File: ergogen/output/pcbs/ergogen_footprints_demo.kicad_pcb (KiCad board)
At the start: 2 copper layers, 99.5 x 99.5 mm, 30 parts

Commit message: Refresh output
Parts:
- added DISP1, DISP2: , ceoloide:nice_view, F.Cu at (75.0, 75.0)
- added DISP3, DISP4, DISP5: , ceoloide:display_ssd1306_nice_view, F.Cu at (75.0, 75.0)
- added JST1: , ceoloide/battery_connector_jst_ph_2, F.Cu at (75.0, 75.0)
- added LED1: , ceoloide:led_SK6812mini-e (per-keysingle-side), B.Cu at (55.0, 50.3)
- added LED2: , ceoloide:led_SK6812mini-e (per-key, reversible), B.Cu at (55.0, 70.3)
- added LED3: , ceoloide:led_SK6812mini-e (underglow, reversible), B.Cu at (35.0, 70.3)
- added LED4: , ceoloide:led_SK6812mini-e (underglowsingle-side), B.Cu at (35.0, 30.3)
- added MCU1, MCU2: , ceoloide:nice_nano, F.Cu at (75.0, 75.0)
- added MH1, MH2: , ceoloide:mounting_hole_npth, F.Cu at (75.0, 75.0)
- added PWR1, PWR2: reset_button, ceoloide:power_switch_smd_side, F.Cu at (75.0, 75.0)
- added RST1, RST2: reset_button_smd_side, ceoloide:reset_button_smd_side, F.Cu at (75.0, 75.0)
- added RST3: reset_switch_tht_top, ceoloide:reset_switch_tht_top, F.Cu at (75.0, 75.0)
- added TRRS1: TRRS-PJ-320A-dual, ceoloide:trrs_pj320a (reversible), F.Cu at (75.0, 75.0)
- added TRRS2: TRRS-PJ-320A-dual, ceoloide:trrs_pj320a (reversible, symmetric), F.Cu at (75.0, 75.0)
- added TRRS3: TRRS-PJ-320A-dual, ceoloide:trrs_pj320a, F.Cu at (75.0, 75.0)
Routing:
- net LED_U_1: track 0.00 -> 209.9 mm, vias 0 -> 1
- net c1_r2: track 0.00 -> 202.8 mm
- net LED_U_2: track 0.00 -> 108.5 mm, vias 0 -> 1
- net LED_U_3: track 0.00 -> 101.8 mm
- net JST1_1: track 0.00 -> 34.3 mm
- net c1_r1: track 0.00 -> 30.7 mm
- net GND: track 0.00 -> 17.3 mm, vias 0 -> 2
- net SDA: track 0.00 -> 9.80 mm
- net SCL: track 0.00 -> 9.80 mm
- net CS: track 0.00 -> 9.80 mm
- net VCC: track 0.00 -> 7.51 mm, vias 0 -> 2
- net LED_1: track 0.00 -> 6.76 mm, vias 0 -> 1
- net LED: track 0.00 -> 6.76 mm, vias 0 -> 1
- net JST1_2: track 0.00 -> 3.60 mm
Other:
- board text added: "JLCJLCJLCJLC"

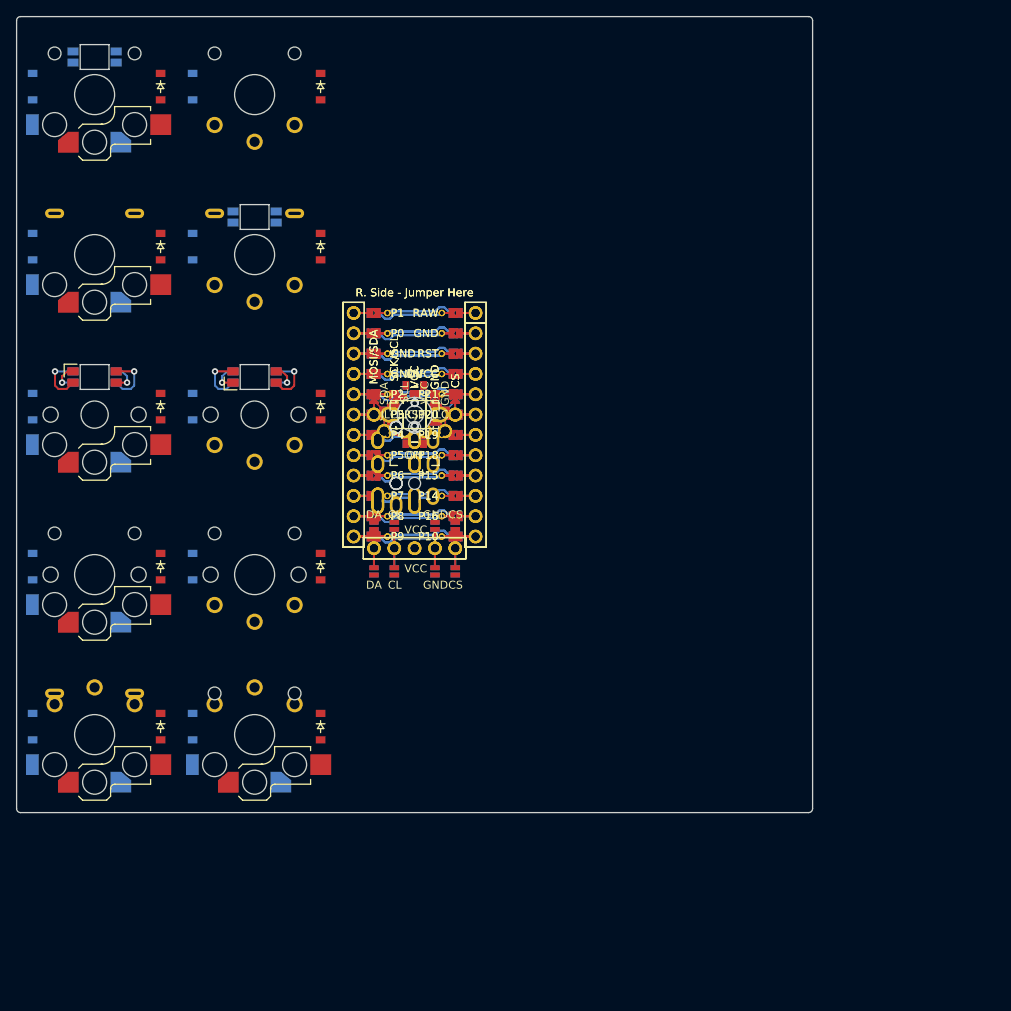
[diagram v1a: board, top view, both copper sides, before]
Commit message: Add some rotation and shift to test footprints
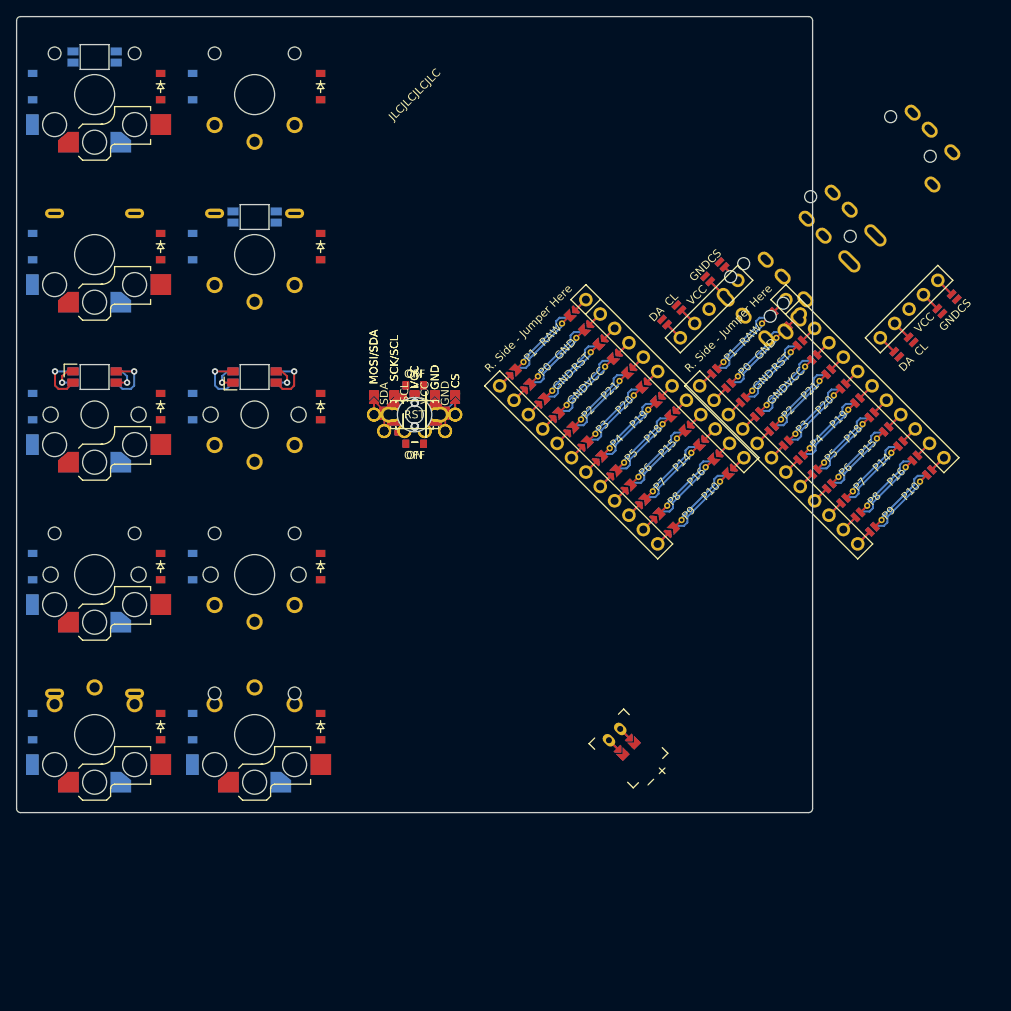
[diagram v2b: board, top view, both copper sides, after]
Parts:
- moved TRRS3 72.1 mm to (135.0, 35.0), turned to 45 degrees
- moved TRRS2 58.3 mm to (125.0, 45.0), turned to 45 degrees
- moved DISP2 55.9 mm to (125.0, 50.0), turned to 45 degrees
- moved MCU2 50.0 mm to (125.0, 75.0), turned to 45 degrees
- moved JST1 47.2 mm to (100.0, 115.0), turned to 45 degrees
- moved TRRS1 44.7 mm to (115.0, 55.0), turned to 45 degrees
- moved DISP1 35.4 mm to (100.0, 50.0), turned to 45 degrees
- moved MCU1 25.0 mm to (100.0, 75.0), turned to 45 degrees

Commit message: Adjust the position of a few components
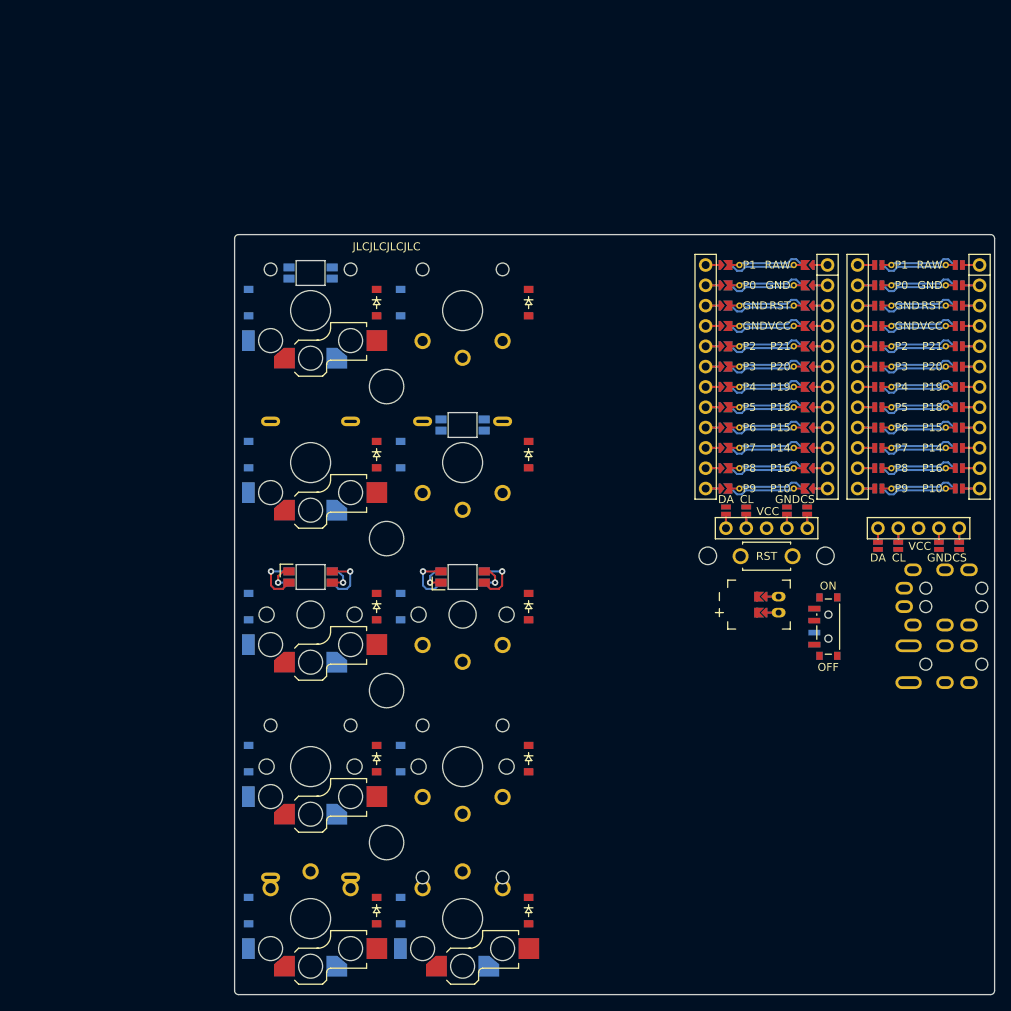
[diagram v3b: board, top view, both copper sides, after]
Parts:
- removed DISP3, DISP4, DISP5: , ceoloide:display_ssd1306_nice_view
- removed PWR2: reset_button, ceoloide:power_switch_smd_side
- removed the RST1 at (75.0, 75.0)
- removed RST2: reset_button_smd_side, ceoloide:reset_button_smd_side
- removed TRRS3: TRRS-PJ-320A-dual, ceoloide:trrs_pj320a
- added MH3: , ceoloide:mounting_hole_npth, F.Cu at (71.5, 90.5)
- added MH4: , ceoloide:mounting_hole_npth, F.Cu at (71.5, 71.5)
- added MH5: , ceoloide:mounting_hole_npth, F.Cu at (111.7, 92.7)
- added MH6: , ceoloide:mounting_hole_npth, F.Cu at (126.3, 92.7)
- moved TRRS2 67.4 mm to (147.5, 108.5), turned to -90 degrees
- moved PWR1 58.1 mm to (126.7, 101.5)
- moved TRRS1 54.7 mm to (147.5, 99.0), turned to -90 degrees
- moved MH1 53.6 mm to (71.5, 128.5)
- moved RST1 47.4 mm to (119.0, 92.7)
- moved DISP1 44.2 mm to (138.0, 72.5), turned to 0 degrees
- moved MCU1 38.5 mm to (138.0, 69.0), turned to 0 degrees
- moved D15 38.2 mm to (70.2, 61.0)
- moved D5 38.2 mm to (54.2, 61.0)
- moved S1 38.2 mm to (62.0, 62.0)
- moved LED4 38.2 mm to (62.0, 57.3)
- moved D10 37.5 mm to (73.2, 61.0)
- moved D14 37.5 mm to (70.2, 80.0)
- moved D20 37.5 mm to (89.2, 61.0)
- moved D4 37.5 mm to (54.2, 80.0)
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- renumbered RST3 to RST1
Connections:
- DISP1 pad 10: DISP1_1 -> CS
- DISP1 pad 11: DISP1_2 -> GND
- DISP1 pad 12: DISP1_4 -> SCL
- DISP1 pad 13: DISP1_5 -> SDA
- DISP1 pad 14: CS -> DISP1_1
- DISP1 pad 15: GND -> DISP1_2
- DISP1 pad 16: SCL -> DISP1_4
- DISP1 pad 17: SDA -> DISP1_5
- DISP1 pad 20: DISP1_5 -> CS
- DISP1 pad 21: DISP1_4 -> GND
- DISP1 pad 22: DISP1_2 -> SCL
- DISP1 pad 23: DISP1_1 -> SDA
- DISP1 pad 24: CS -> DISP1_5
- DISP1 pad 25: GND -> DISP1_4
- DISP1 pad 26: SCL -> DISP1_2
- DISP1 pad 27: SDA -> DISP1_1
- DISP2 pad 10: CS -> DISP2_1
- DISP2 pad 11: GND -> DISP2_2
- DISP2 pad 12: SCL -> DISP2_4
- DISP2 pad 13: SDA -> DISP2_5
- DISP2 pad 14: DISP2_1 -> CS
- DISP2 pad 15: DISP2_2 -> GND
- DISP2 pad 16: DISP2_4 -> SCL
- DISP2 pad 17: DISP2_5 -> SDA
- DISP2 pad 20: CS -> DISP2_5
- DISP2 pad 21: GND -> DISP2_4
- DISP2 pad 22: SCL -> DISP2_2
- DISP2 pad 23: SDA -> DISP2_1
- DISP2 pad 24: DISP2_5 -> CS
- DISP2 pad 25: DISP2_4 -> GND
- DISP2 pad 26: DISP2_2 -> SCL
- DISP2 pad 27: DISP2_1 -> SDA
- MCU1 pad 1: MCU1_1 -> RAW
- MCU1 pad 10: MCU1_10 -> P14
- MCU1 pad 11: MCU1_11 -> P16
- MCU1 pad 12: MCU1_12 -> P10
- MCU1 pad 13: MCU1_13 -> MCU1_12
- MCU1 pad 14: MCU1_14 -> MCU1_11
- MCU1 pad 15: MCU1_15 -> MCU1_10
- MCU1 pad 16: MCU1_16 -> MCU1_9
- MCU1 pad 17: MCU1_17 -> MCU1_8
- MCU1 pad 18: MCU1_18 -> MCU1_7
- MCU1 pad 19: MCU1_19 -> MCU1_6
- MCU1 pad 2: MCU1_2 -> GND
- MCU1 pad 20: MCU1_20 -> MCU1_5
- MCU1 pad 21: MCU1_21 -> MCU1_4
- MCU1 pad 22: MCU1_22 -> MCU1_3
- MCU1 pad 23: MCU1_23 -> MCU1_2
- MCU1 pad 24: MCU1_24 -> MCU1_1
- MCU1 pad 3: MCU1_3 -> RST
- MCU1 pad 4: MCU1_4 -> VCC
- MCU1 pad 5: MCU1_5 -> P21
- MCU1 pad 6: MCU1_6 -> P20
- MCU1 pad 7: MCU1_7 -> P19
- MCU1 pad 8: MCU1_8 -> P18
- MCU1 pad 9: MCU1_9 -> P15
- MCU2 pad 1: RAW -> MCU2_1
- MCU2 pad 10: P14 -> MCU2_10
- MCU2 pad 11: P16 -> MCU2_11
- MCU2 pad 12: P10 -> MCU2_12
- MCU2 pad 13: MCU2_12 -> MCU2_13
- MCU2 pad 14: MCU2_11 -> MCU2_14
- MCU2 pad 15: MCU2_10 -> MCU2_15
- MCU2 pad 16: MCU2_9 -> MCU2_16
- MCU2 pad 17: MCU2_8 -> MCU2_17
- MCU2 pad 18: MCU2_7 -> MCU2_18
- MCU2 pad 19: MCU2_6 -> MCU2_19
- MCU2 pad 2: GND -> MCU2_2
- MCU2 pad 20: MCU2_5 -> MCU2_20
- MCU2 pad 21: MCU2_4 -> MCU2_21
- MCU2 pad 22: MCU2_3 -> MCU2_22
- MCU2 pad 23: MCU2_2 -> MCU2_23
- MCU2 pad 24: MCU2_1 -> MCU2_24
- MCU2 pad 3: RST -> MCU2_3
- MCU2 pad 4: VCC -> MCU2_4
- MCU2 pad 5: P21 -> MCU2_5
- MCU2 pad 6: P20 -> MCU2_6
- MCU2 pad 7: P19 -> MCU2_7
- MCU2 pad 8: P18 -> MCU2_8
- MCU2 pad 9: P15 -> MCU2_9
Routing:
- net P21: track 0.00 -> 203.1 mm
- net LED_U_1: track 209.9 -> 6.76 mm
- net P18: track 0.00 -> 101.8 mm
- net P15: track 0.00 -> 101.8 mm
- net LED_U_3: track 101.8 -> 0.00 mm
- net LED_U_2: track 108.5 -> 6.76 mm
- net JST1_1: track 34.3 -> 3.60 mm
- net GND: track 17.3 -> 45.2 mm
- net SCL: track 9.80 -> 7.00 mm
- net CS: track 9.80 -> 7.00 mm
- net SDA: track 9.80 -> 7.00 mm
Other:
- board size 99.5 x 99.5 mm -> 95 x 95 mm

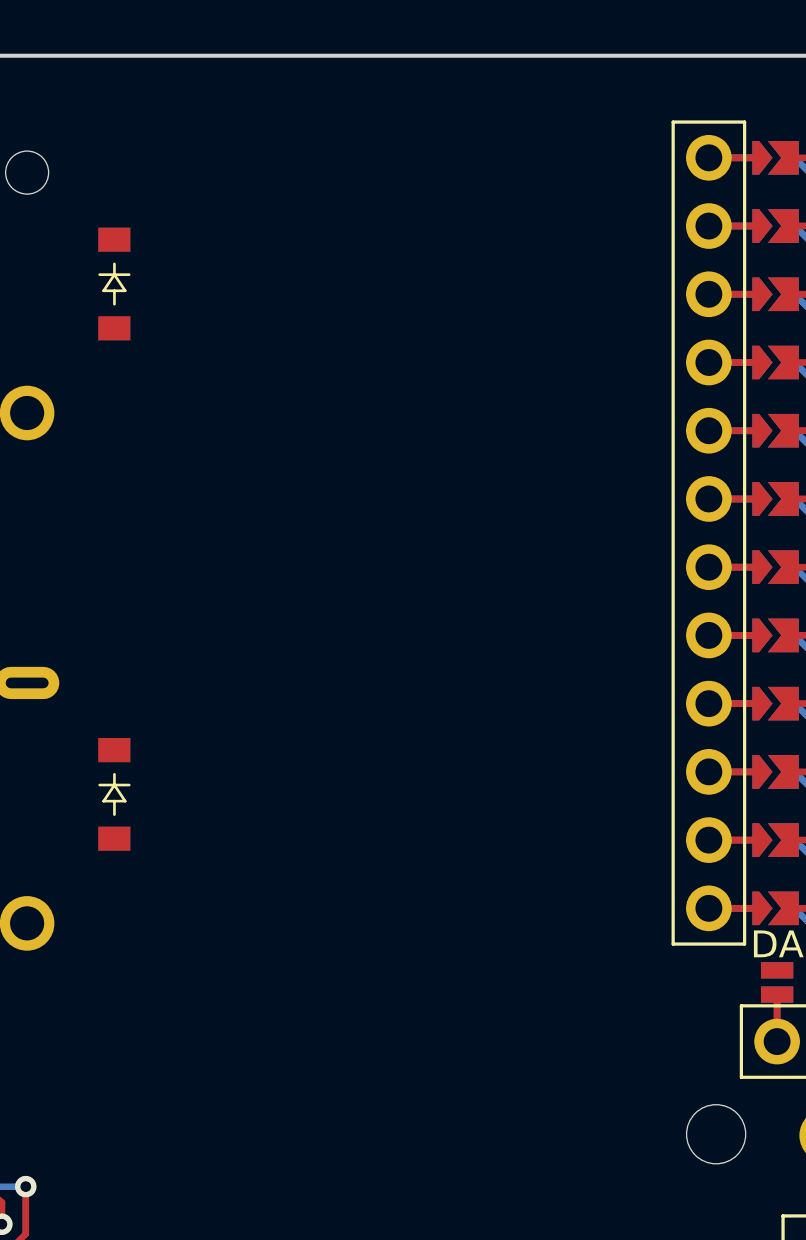
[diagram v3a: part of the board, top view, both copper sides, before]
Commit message: Add nice_nano with only required jumpers
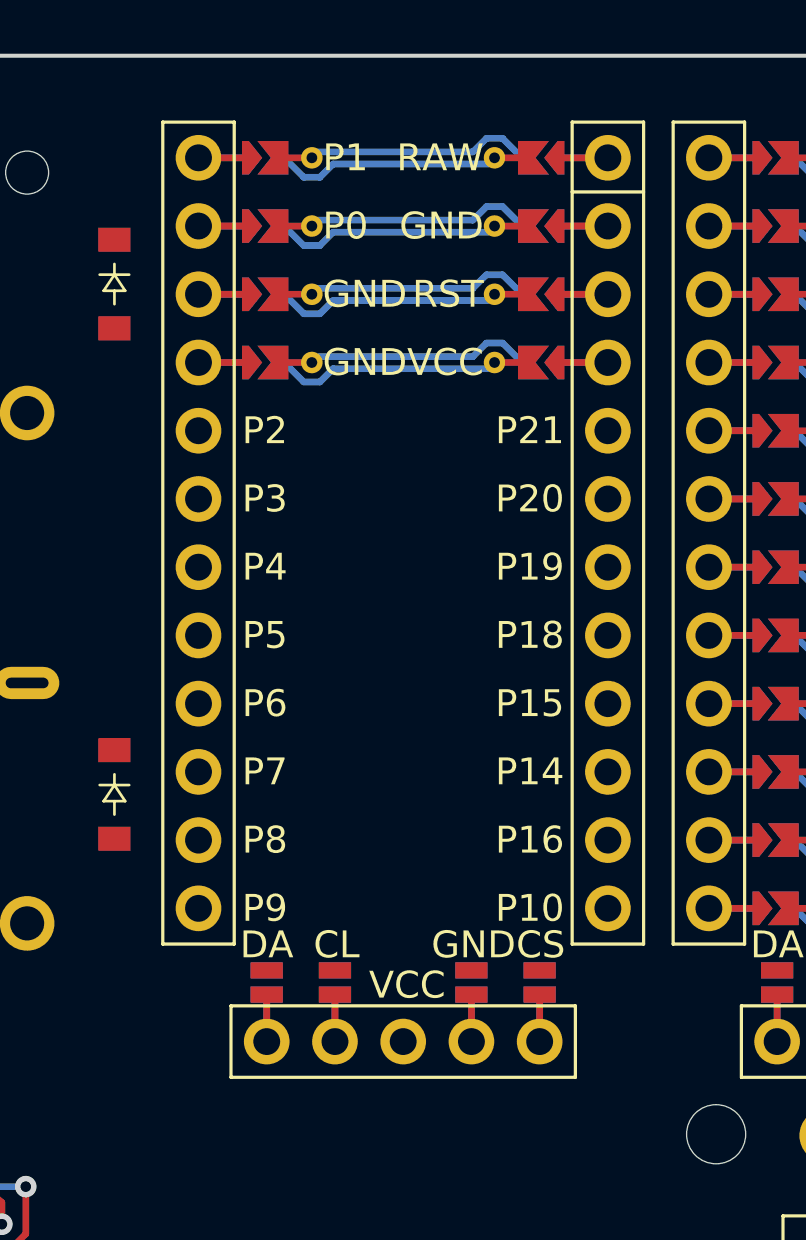
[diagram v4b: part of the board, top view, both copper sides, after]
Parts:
- added DISP3: , ceoloide:nice_view, F.Cu at (100.0, 72.5)
- added MCU3: , ceoloide:nice_nano, F.Cu at (100.0, 69.0)
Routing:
- net P21: track 203.1 -> 237.0 mm
- net c1_r2: track 202.8 -> 236.6 mm
- net P18: track 101.8 -> 118.7 mm
- net P15: track 101.8 -> 118.7 mm
- net GND: track 45.2 -> 54.2 mm
- net c1_r1: track 30.7 -> 36.2 mm
- net SDA: track 7.00 -> 10.5 mm
- net SCL: track 7.00 -> 10.5 mm
- net CS: track 7.00 -> 10.5 mm

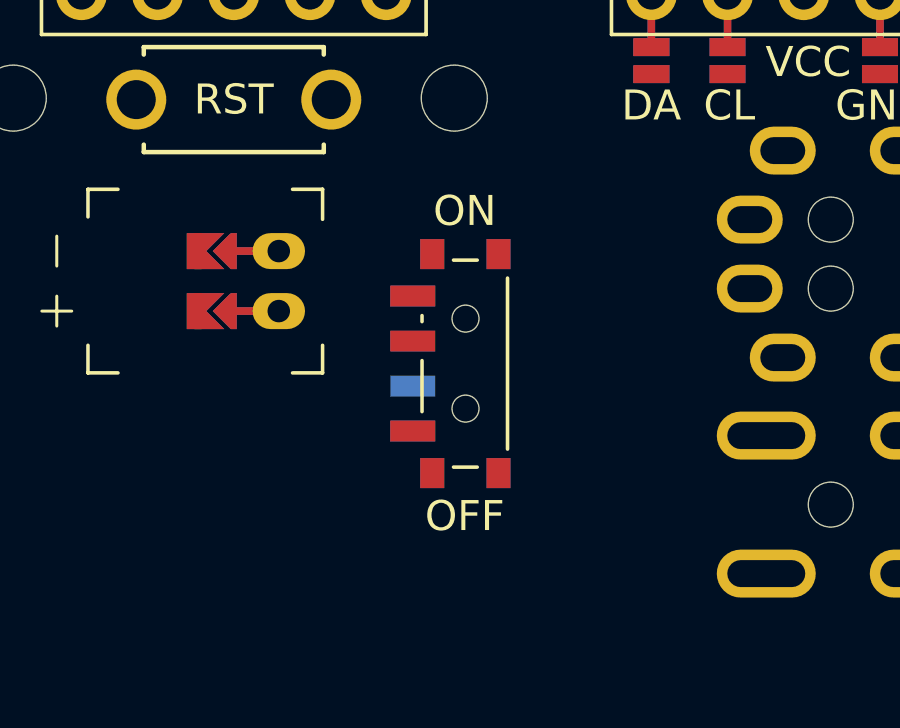
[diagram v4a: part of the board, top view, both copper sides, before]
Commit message: Slightly adjust power switch
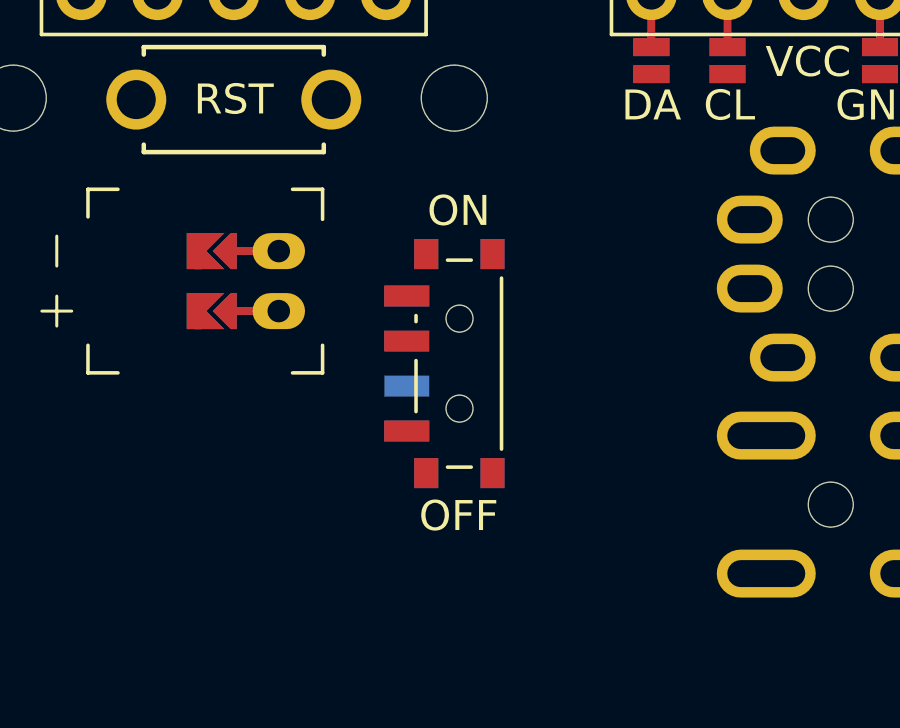
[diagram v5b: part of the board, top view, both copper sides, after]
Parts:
- moved PWR1 0.20 mm to (126.5, 101.5)
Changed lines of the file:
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@@
         (segment (start 118.700 99.750) (end 120.500 99.750) (width 0.25) (layer "B.Cu") (net 99))
       (module "ceoloide:power_switch_smd_side" (layer F.Cu)
-        (at 126.7 101.5 0)
+        (at 126.5 101.5 0)
         (attr smd)
         (fp_text value "reset_button" (at 0 2.5 0) (layer F.Fab)
